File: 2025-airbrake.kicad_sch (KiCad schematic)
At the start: 11 parts, among them J1 SERVO, J2 JST-DY, J3 POWER_SEL, U1 STM32F411 Black Pill, U2 SPI Flash W25Q128JV, U3 Adafruit Micro SD Breakout, U4 MS5611, U5 NeoPixel Stick, U6 BNO055 Breakout, U7 MP2307 EVAL, U8 RFD900X

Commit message: Routing
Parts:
- U7: footprint Connector_PinHeader_2.54mm:PinHeader_2x02_P2.54mm_Vertical -> Connector_PinHeader_2.54mm:PinHeader_1x03_P2.54mm_Vertical
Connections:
- net +3V3: now also U1.18 (3V3); no longer U1.40 (3V3)
- net +5V: now also U7.2 (5V), U8.5 (VUSB), U8.6 (VUSB); no longer U1.38 (5V), U7.1 (5V)
- net +BATT: now also U7.3 (BATT_POS); no longer U7.4 (BATT_POS)
- net CS-FLASH: now also U1.9 (PA3); no longer U1.35 (PB7)
- net CS-SD: now also U1.6 (PA0); no longer U1.34 (PB6)
- net GND: now also U7.1 (GND); no longer U7.2 (GND), U7.3 (GND)
- net BNO_RST: now reaches U6.6 (RST)
- net BNO_RST: now also U1.14 (PB0)
- no-connect marks 48 -> 45

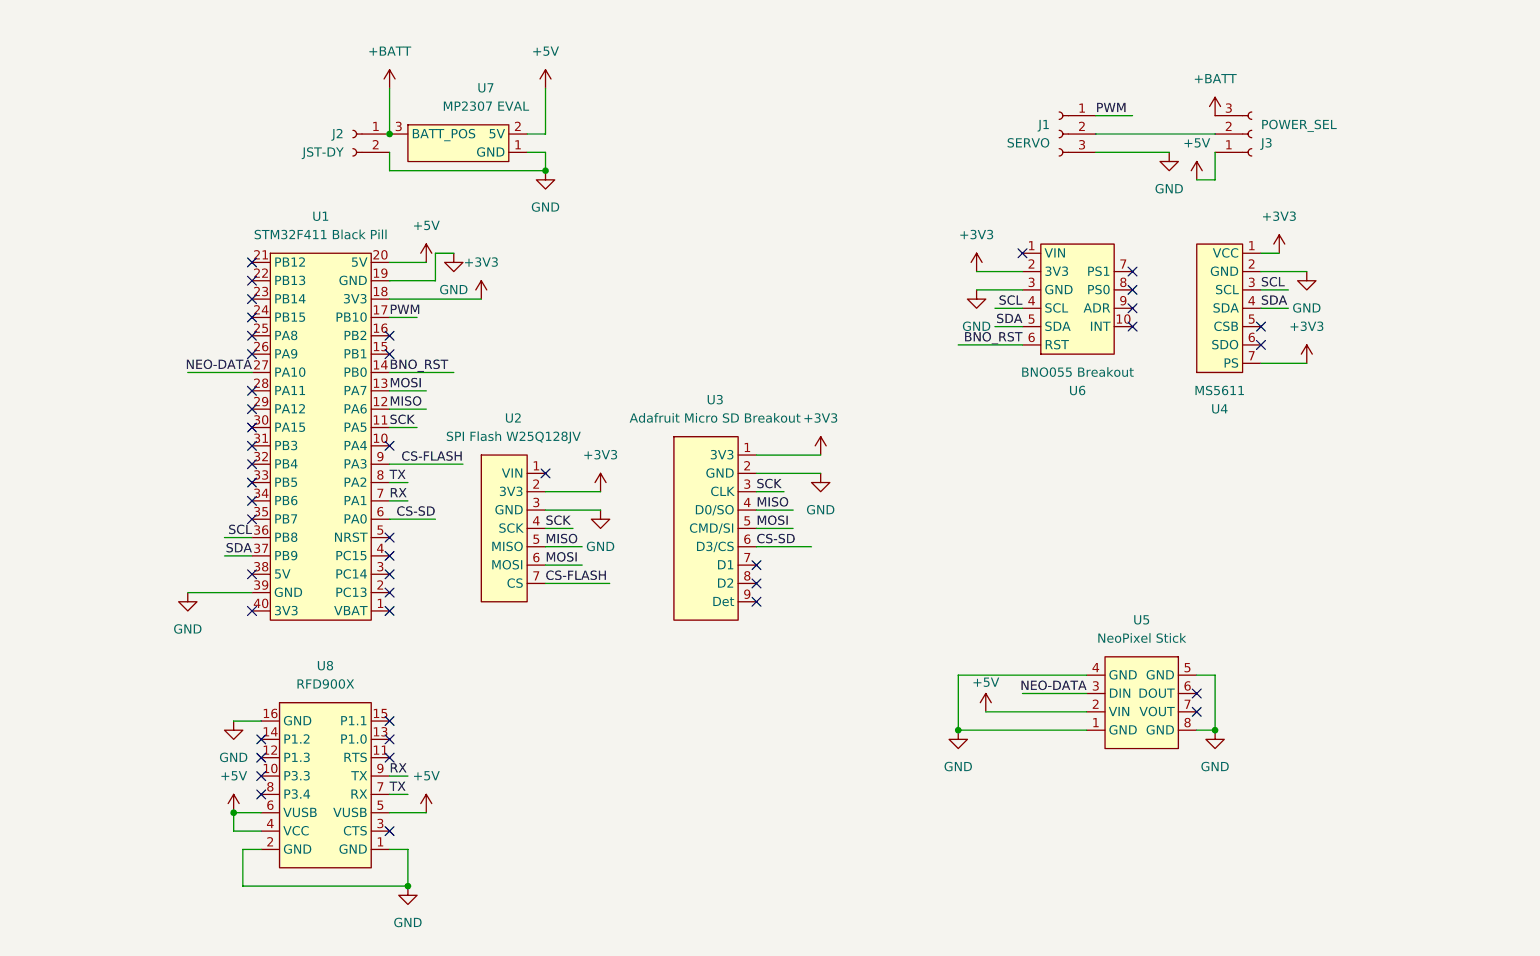
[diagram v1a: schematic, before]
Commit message: Added symbols and heiarchy
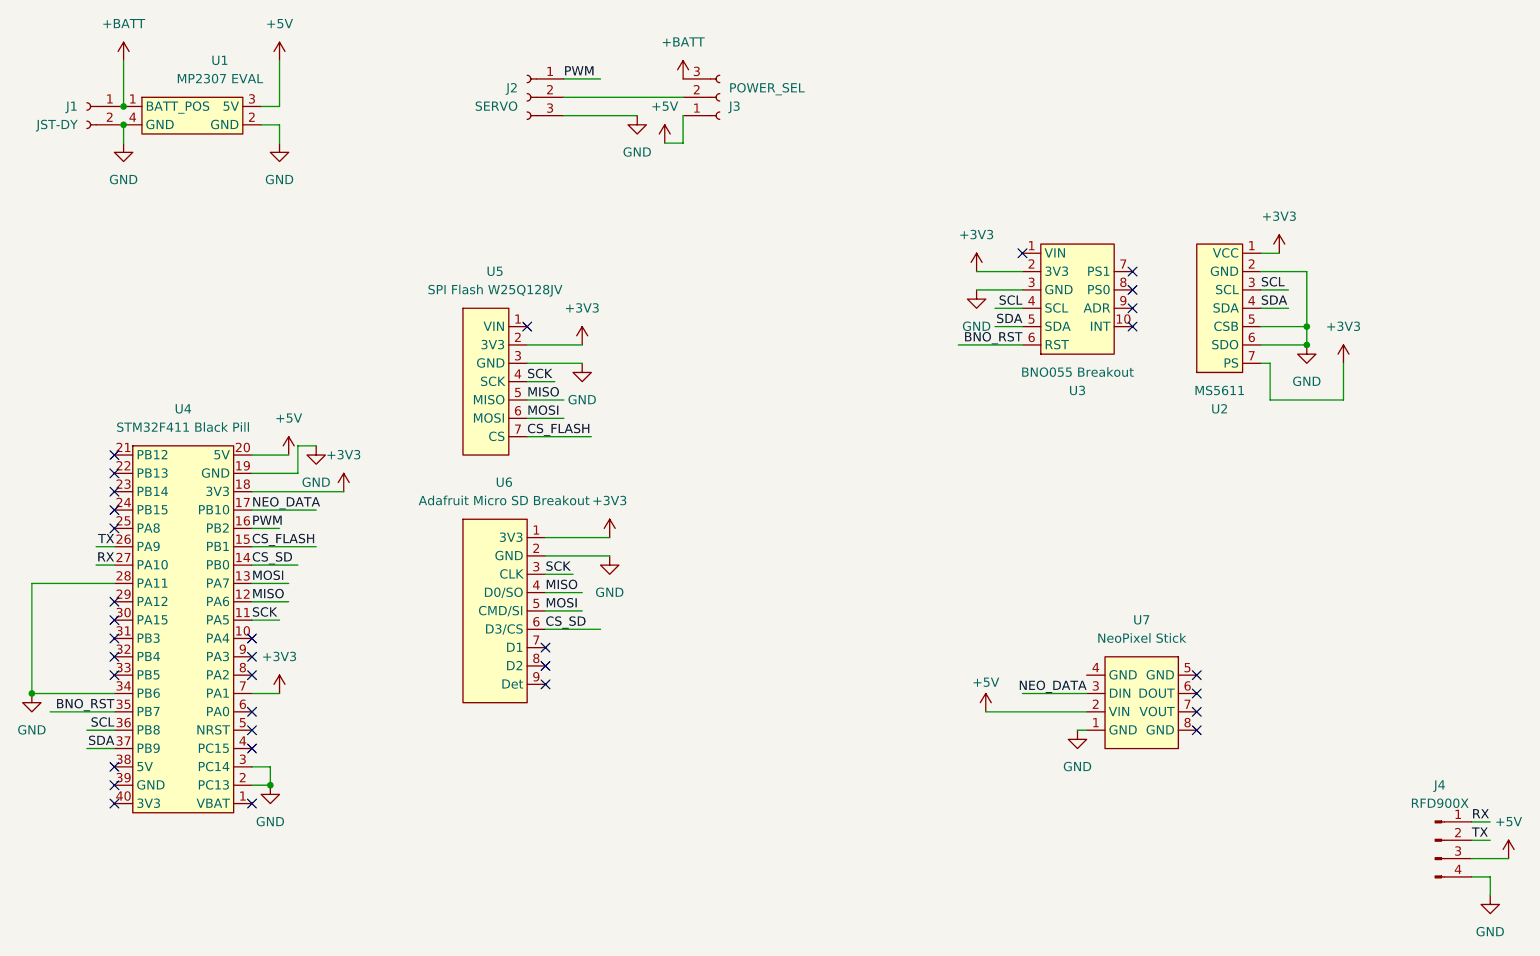
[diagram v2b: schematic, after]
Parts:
- removed U8: RFD900X, Connector_PinSocket_2.54mm:PinSocket_2x08_P2.54mm_Horizontal, symbol 2025-airbrakes:RFD900X
- added J4: RFD900X, Connector_PinHeader_2.54mm:PinHeader_1x04_P2.54mm_Horizontal, symbol Connector:Conn_01x04_Pin
- U1: renamed from U7; footprint Connector_PinHeader_2.54mm:PinHeader_1x03_P2.54mm_Vertical -> Connector_PinHeader_2.54mm:PinHeader_2x02_P2.54mm_Vertical
- renumbered J2 to J1, J1 to J2, U4 to U2, U6 to U3, U1 to U4, U2 to U5, U3 to U6, U5 to U7
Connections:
- net +3V3: now also U4.7 (PA1)
- net +5V: now also U1.3 (5V), J4.3 (Pin_3); no longer U1.2 (5V)
- net +BATT: now also U1.1 (BATT_POS); no longer U1.3 (BATT_POS)
- net BNO_RST: now also U4.35 (PB7); no longer U4.14 (PB0)
- net GND: now also U1.2 (GND), U1.4 (GND), U2.5 (CSB), U2.6 (SDO), U4.2 (PC13), U4.28 (PA11), U4.3 (PC14), U4.34 (PB6), J4.4 (Pin_4); no longer U1.1 (GND), U4.39 (GND), U7.4 (GND), U7.5 (GND), U7.8 (GND)
- net PWM: now also U4.16 (PB2); no longer U4.17 (PB10)
- net RX: now also U4.27 (PA10), J4.1 (Pin_1); no longer U4.7 (PA1)
- net TX: now also U4.26 (PA9), J4.2 (Pin_2); no longer U4.8 (PA2)
- net CS_FLASH: now reaches U4.15 (PB1)
- net CS_FLASH: now also U5.7 (CS)
- net CS-FLASH: no longer names the net of U4.9 (PA3)
- net CS-FLASH: no longer U5.7 (CS)
- net CS-SD: no longer names the net of U4.6 (PA0)
- net CS-SD: no longer U6.6 (D3/CS)
- net NEO-DATA renamed NEO_DATA
- net NEO_DATA: now also U4.17 (PB10); no longer U4.27 (PA10)
- new net CS_SD: U4.14 (PB0), U6.6 (D3/CS)
- no-connect marks 45 -> 33
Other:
- moved on the sheet: J1, J2, J3, U4, U5, U6
